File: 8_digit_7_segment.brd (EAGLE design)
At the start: 100.3 x 36.6 mm, 9 parts, among them IC1 MAX7219CNG

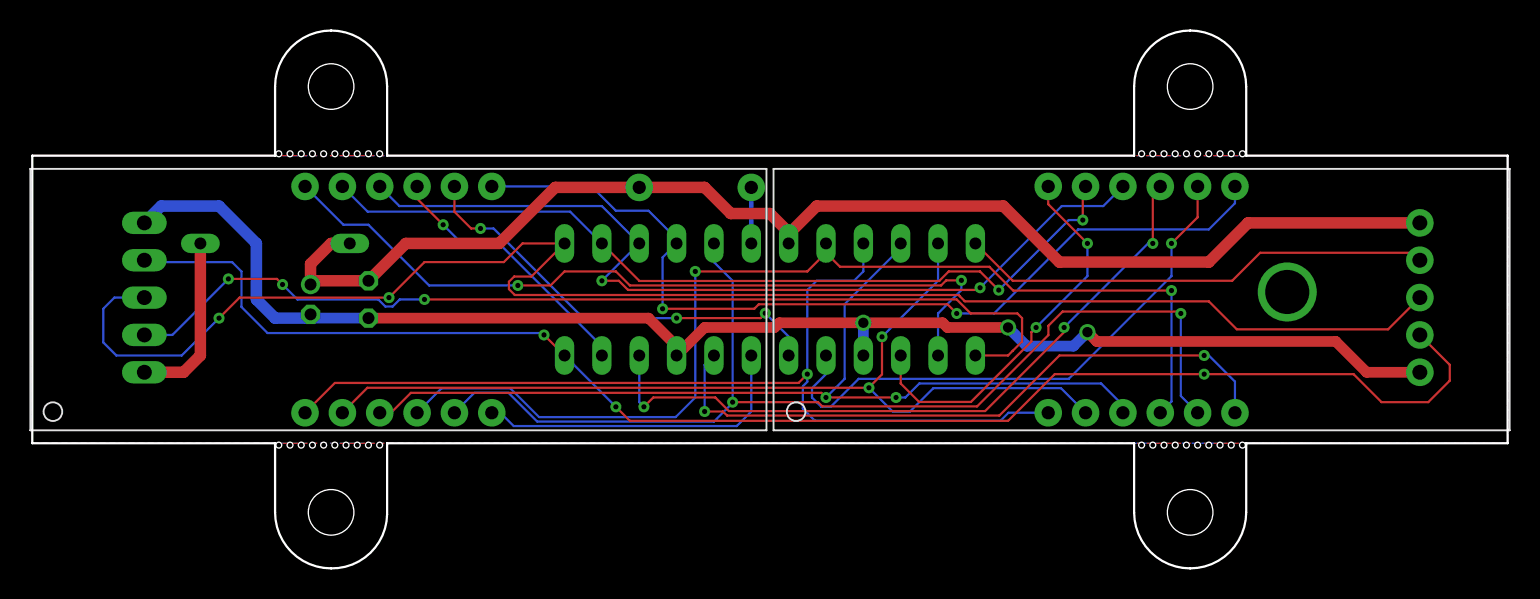
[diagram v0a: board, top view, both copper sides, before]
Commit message: Minor modifications, 3D components added to the Eagle files and new images added of the 3D model
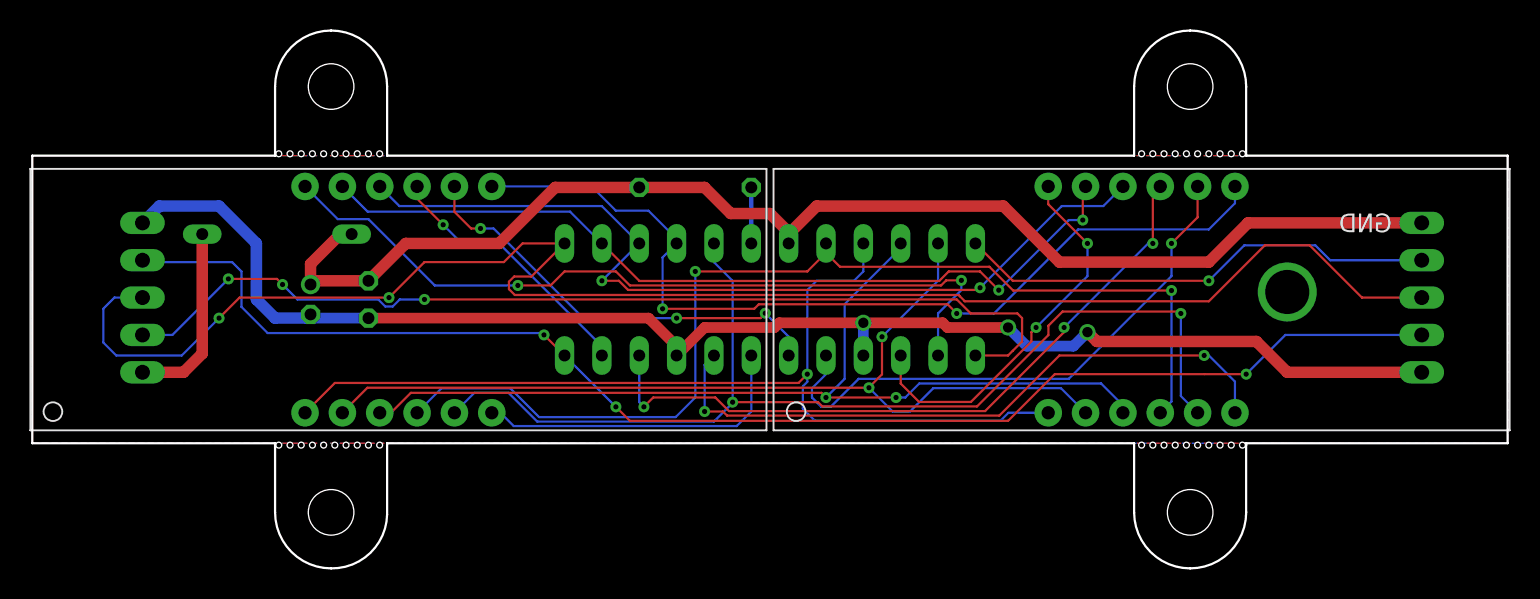
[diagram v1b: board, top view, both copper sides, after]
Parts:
- C1: device 001-private-inventory:C025-024X044 -> 006-rcl:C025-024X044
- C3: device 001-private-inventory:E2-4 -> 006-rcl:E2-5
- D1: device diode:DO35-10 -> 13-diode:D-10
- IC1: value MAX7219CNG -> IC_MAX7219CNG; device maxim:DIL24-3 -> 14-displays:DIL24-3
- OUTPUT: device SparkFun-Connectors:1X05 -> 007-connectors:1X05/90FEMALE
- R1: device SparkFun-Resistors:AXIAL-0.3 -> 006-rcl:0207/7
- moved OUTPUT 6.43 mm to (80.5, 34.4)
- moved D1 0.65 mm to (-1.14, 38.7)
- moved INPUT 0.13 mm to (-14.1, 34.4)
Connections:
- net ISET: now also R1.2; no longer R1.P$2
- net VCC: now also R1.1; no longer R1.P$1
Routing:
- net CS: track 101.4 -> 95.4 mm
- net CLK: track 109.6 -> 111.0 mm
- net VIN: track 11.9 -> 12.7 mm
- net DOUT: track 32.3 -> 32.8 mm, vias 0 -> 1
- net VCC: track 88.9 -> 89.5 mm
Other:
- board text added: "CLK"
- board text added: "CS"
- board text added: "DIN"
- board text added: "DOUT"
- board text added: "GND"
- board text added: "VCC"
